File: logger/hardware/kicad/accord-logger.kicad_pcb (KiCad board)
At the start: 2 copper layers, 120 x 80 mm, 40 parts, among them J1 Board connector 14-way, J5 SD breakout 6-way, Q5 IPD50P04P4L-11, Q6 2N3904, Q7 2N3904, U1 RaspberryPi_Pico_W, U15 MAX3485, U16 DS3231SN, U6 LM2678T-5.0

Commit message: layout: rs485_links step placed and routed
Owner switched on rs485_links (R47-R49, JP2-JP4; six on_board flags).
JP2-JP4 sit in a row at the top edge (y 64), R47/R48 bias and R49
termination between them and U15. Nets checked pad by pad: R47 BIAS_HI-A,
R48 B-BIAS_LO, R49 A-TERM, JP2 TERM-B, JP3 3V3-BIAS_HI, JP4 BIAS_LO-PGND.

Scratch copy refilled: the front pour now has one 45.6 mm2 piece around
U15 (x 148-163, y 64-73) cut off by the new tracks; it is tied to ground
through U15 pin 5 and JP4's through-hole pads, and KiCad's island removal
(always) keeps only connected copper. Two slivers under 1 mm2. DRC
schematic parity 0, no clearance or courtyard errors; unconnected only
AGND (with the inputs) and Q5's middle lead (internal to the part).

Claude-Session-ID: 42dd0e33-28b5-4936-847e-9c2e1d2488fa
Co-Authored-By: Claude Opus 5.5 <noreply@anthropic.com>
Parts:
- added JP2: TERM default OPEN, Connector_PinHeader_2.54mm:PinHeader_1x02_P2.54mm_Vertical, F.Cu at (165.7, 64.1)
- added JP3: BIAS HI default OPEN, Connector_PinHeader_2.54mm:PinHeader_1x02_P2.54mm_Vertical, F.Cu at (169.5, 64.1)
- added JP4: BIAS LO default OPEN, Connector_PinHeader_2.54mm:PinHeader_1x02_P2.54mm_Vertical, F.Cu at (173.4, 64.1)
- added R47: 390R, Resistor_THT:R_Axial_DIN0207_L6.3mm_D2.5mm_P5.08mm_Vertical, F.Cu at (165.3, 71.8)
- added R48: 390R, Resistor_THT:R_Axial_DIN0207_L6.3mm_D2.5mm_P5.08mm_Vertical, F.Cu at (165.3, 75.6)
- added R49: 120R, Resistor_THT:R_Axial_DIN0207_L6.3mm_D2.5mm_P5.08mm_Vertical, F.Cu at (156.4, 66.0)
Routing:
- net /P3V3_SW: track 104.3 -> 138.0 mm
- net /RS485_B: track 55.2 -> 85.7 mm
- net /RS485_A: track 55.2 -> 83.1 mm
- net /RS485_BIAS_LO: track 0.00 -> 13.9 mm
- net /RS485_BIAS_HI: track 0.00 -> 6.83 mm
- net /RS485_TERM: track 0.00 -> 5.01 mm

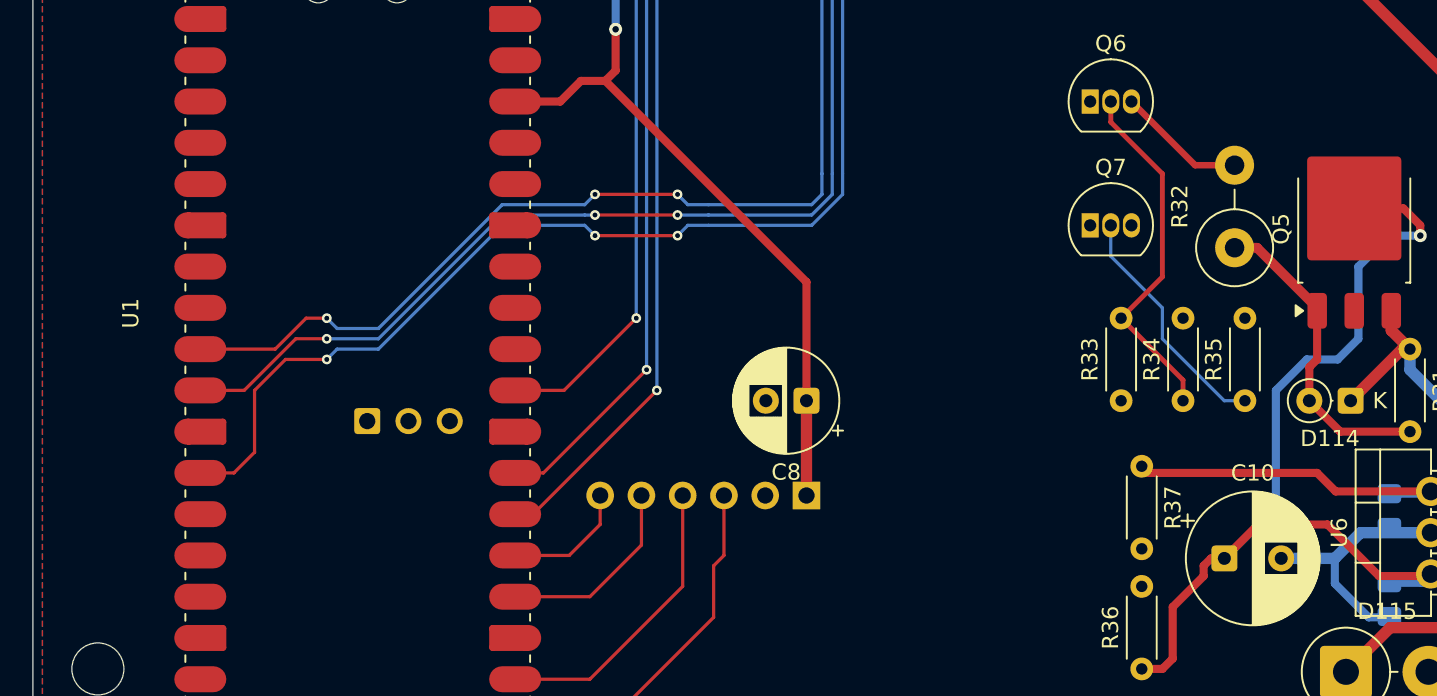
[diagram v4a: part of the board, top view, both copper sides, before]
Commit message: layout: headers step placed and routed
Owner switched on the headers step (J3, J4, TP24, TP25; four on_board
flags). J3 and the GP11/GP12 pads sit in the free strip left of the Pico
above the antenna end (J3 pin 4 at y 127.6, 7.3 mm from GP13); J4 is
13 mm from RUN. A missing via left U15 VCC, C24 and J3 pin 3 off 3V3 on
the first pass; with it added, a copper flood from U15 pin 8 reaches
every P3V3_SW pad including Pico pin 36.

Scratch copy refilled: DRC schematic parity 0, no clearance, courtyard
or dangling-track items; unconnected only AGND (with the inputs) and Q5's
middle lead (internal to the part). Saved with the zone unfilled.

Claude-Session-ID: 42dd0e33-28b5-4936-847e-9c2e1d2488fa
Co-Authored-By: Claude Opus 5.5 <noreply@anthropic.com>
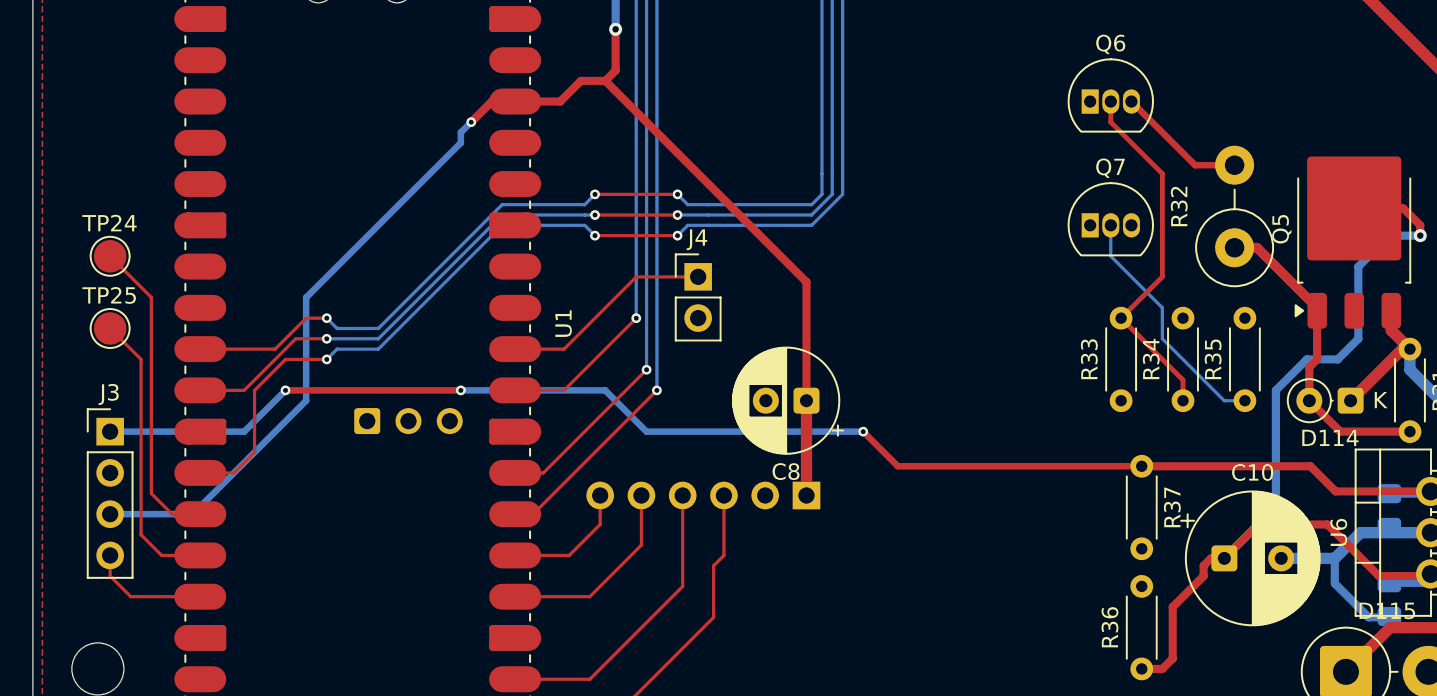
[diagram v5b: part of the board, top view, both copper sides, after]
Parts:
- added J3: Spare GP13 / switched power, Connector_PinHeader_2.54mm:PinHeader_1x04_P2.54mm_Vertical, F.Cu at (93.3, 120.0)
- added J4: Reset RUN-GND, Connector_PinHeader_2.54mm:PinHeader_1x02_P2.54mm_Vertical, F.Cu at (129.5, 110.5)
- added TP24: TestPoint, TestPoint:TestPoint_Pad_D2.0mm, F.Cu at (93.3, 109.2)
- added TP25: TestPoint, TestPoint:TestPoint_Pad_D2.0mm, F.Cu at (93.3, 113.7)
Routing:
- net /B5: track 53.0 -> 119.5 mm, vias 0 -> 3
- net /P3V3_SW: track 138.0 -> 177.6 mm, vias 3 -> 4
- net /SPARE_GP11: track 0.00 -> 19.2 mm
- net /SPARE_GP12: track 0.00 -> 17.7 mm
- net /RUN: track 0.00 -> 13.1 mm
- net /SPARE_GP13: track 0.00 -> 7.35 mm

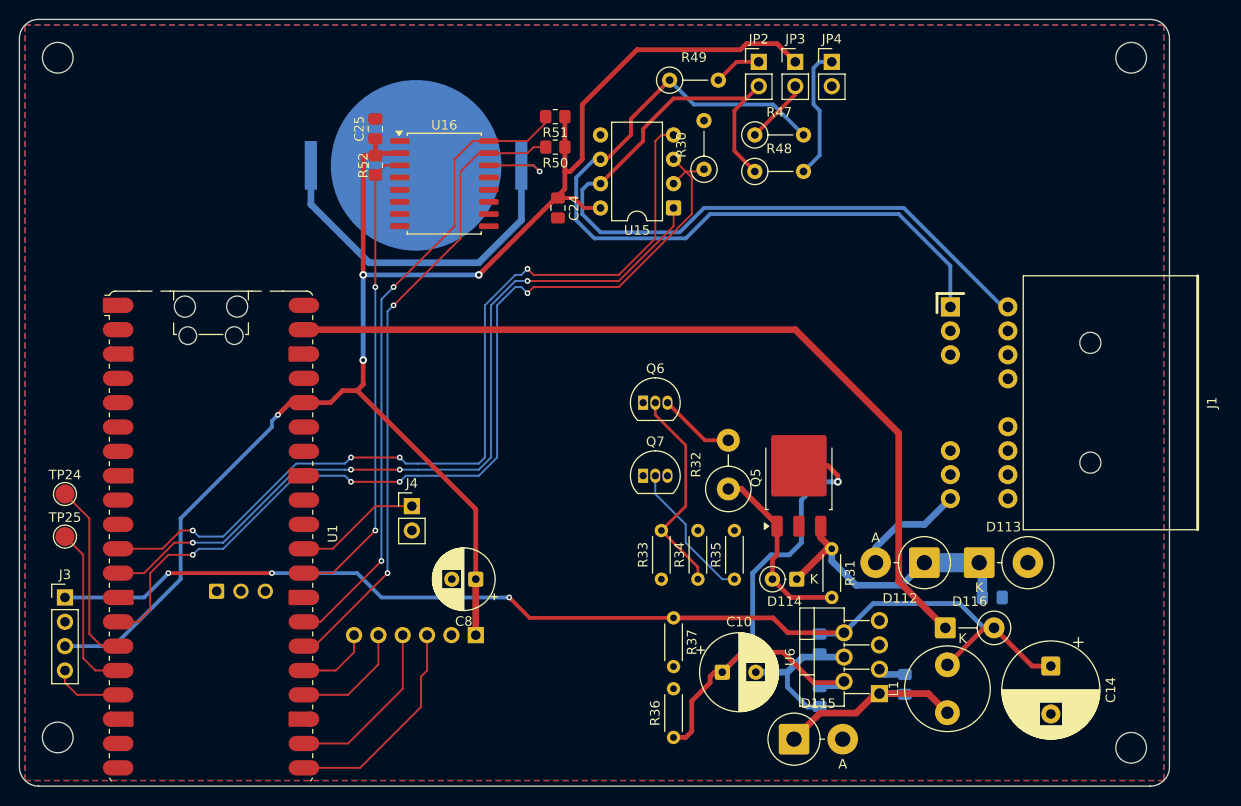
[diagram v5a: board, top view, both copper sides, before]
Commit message: layout: power_tps step placed and routed
Owner switched on power_tps (TP1-TP7, TP21-TP23; ten on_board flags) and
placed each beside its source; D115 moved 1.9 mm left (K to U6.1
11.8 mm, A to C10- 10.0 mm). Copper flood from each test point reaches
its net's parts: TP1 P12 (Q5.3, D112-D114, C9), TP2 GATE, TP3 VIN_SW
(U6.2, C10, C11), TP4 SW (4.5 mm stub), TP5 B5, TP6 VSYS, TP7 3V3 (all
12 pads), TP23 AGND at Pico pin 33.

Open: clearance error, the 0.2 mm B.Cu PGND track from (177.2, 123.8) to
TP22 passes about 0.13 mm from U6 pin 5 (NC); TP22 is a through-hole loop
on the pour, so the track can go. Otherwise DRC (refilled scratch copy)
parity 0; unconnected only AGND to J1.10 (with the inputs) and Q5's
middle lead.

Claude-Session-ID: 42dd0e33-28b5-4936-847e-9c2e1d2488fa
Co-Authored-By: Claude Opus 5.5 <noreply@anthropic.com>
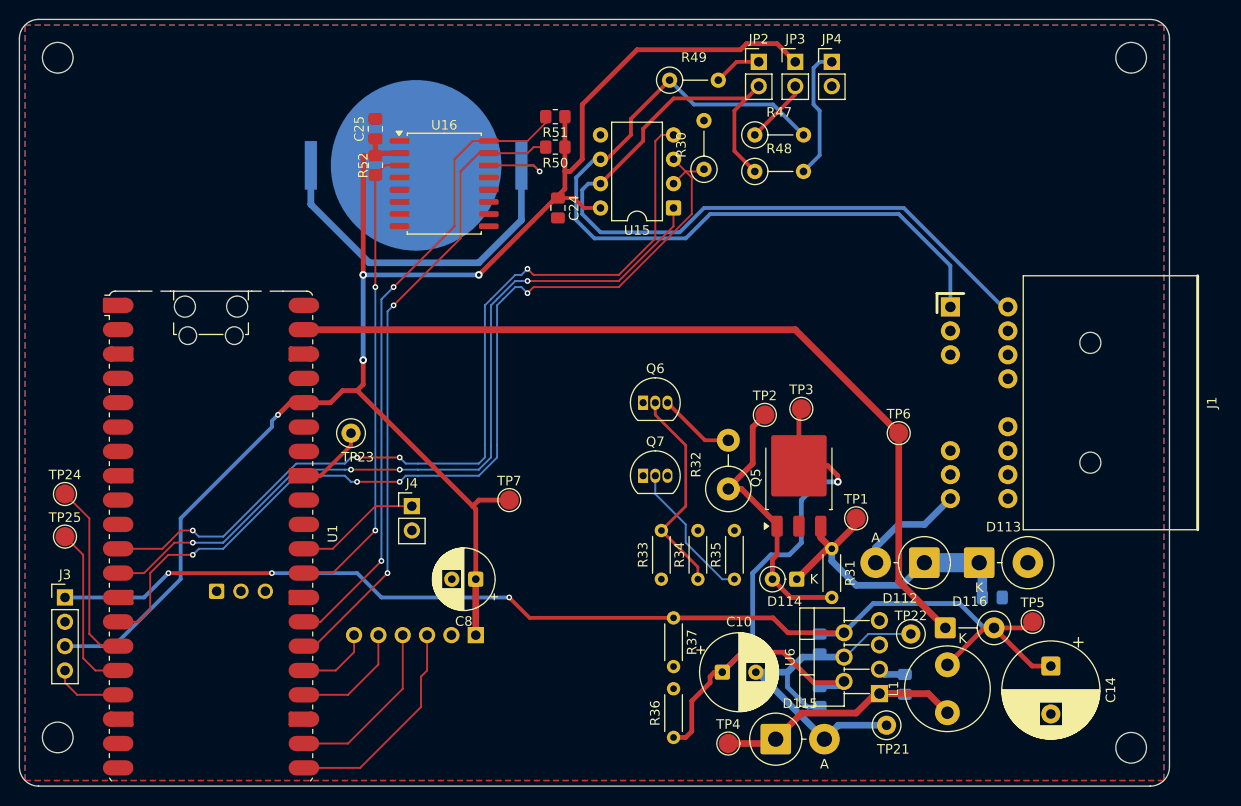
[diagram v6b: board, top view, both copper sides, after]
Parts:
- added TP1: TestPoint, TestPoint:TestPoint_Pad_D2.0mm, F.Cu at (175.9, 111.8)
- added TP2: TestPoint, TestPoint:TestPoint_Pad_D2.0mm, F.Cu at (166.4, 101.0)
- added TP21: TestPoint, TestPoint:TestPoint_Loop_D2.50mm_Drill1.0mm, F.Cu at (179.1, 133.3)
- added TP22: TestPoint, TestPoint:TestPoint_Loop_D2.50mm_Drill1.0mm, F.Cu at (181.6, 123.8)
- added TP23: TestPoint, TestPoint:TestPoint_Loop_D2.50mm_Drill1.0mm, F.Cu at (123.2, 102.9)
- added TP3: TestPoint, TestPoint:TestPoint_Pad_D2.0mm, F.Cu at (170.2, 100.3)
- added TP4: TestPoint, TestPoint:TestPoint_Pad_D2.0mm, F.Cu at (162.6, 135.3)
- added TP5: TestPoint, TestPoint:TestPoint_Pad_D2.0mm, F.Cu at (194.3, 122.6)
- added TP6: TestPoint, TestPoint:TestPoint_Pad_D2.0mm, F.Cu at (180.3, 102.9)
- added TP7: TestPoint, TestPoint:TestPoint_Pad_D2.0mm, F.Cu at (139.7, 109.9)
- moved D115 1.91 mm to (167.5, 134.8)
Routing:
- net /PGND: track 15.6 -> 40.8 mm
- net /GATE: track 19.5 -> 28.8 mm
- net /AGND: track 0.00 -> 7.50 mm
- net /SW: track 21.5 -> 28.5 mm
- net /VIN_SW: track 60.1 -> 66.1 mm
- net /B5: track 119.5 -> 123.8 mm
- net /P12: track 30.3 -> 34.5 mm
- net /P3V3_SW: track 177.6 -> 181.7 mm

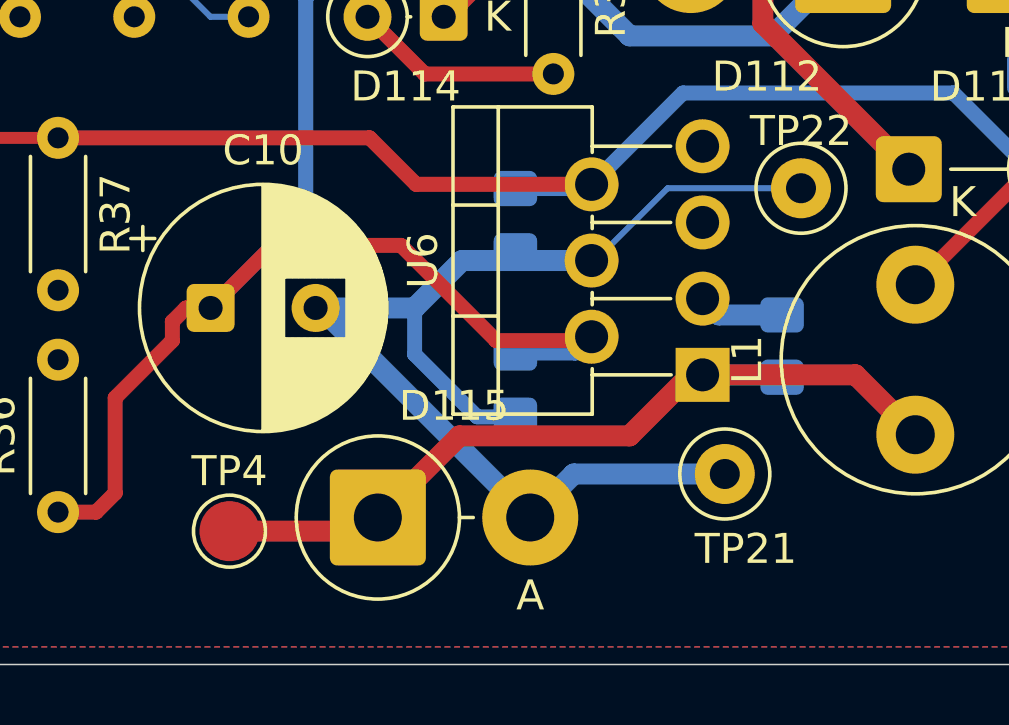
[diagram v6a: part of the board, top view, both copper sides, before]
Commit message: layout: TP4 moved beside U6, TP22 clearance fixed
TP4 (SW) now sits by U6 with about 1.8 mm of stub (was 4.5 mm); the
PGND track that crowded U6 pin 5 is gone and TP21 shifted 0.6 mm. Saved
with the pour filled. DRC: no clearance errors, parity 0, unconnected
only AGND to J1.10 and Q5's middle lead.

Claude-Session-ID: 42dd0e33-28b5-4936-847e-9c2e1d2488fa
Co-Authored-By: Claude Opus 5.5 <noreply@anthropic.com>
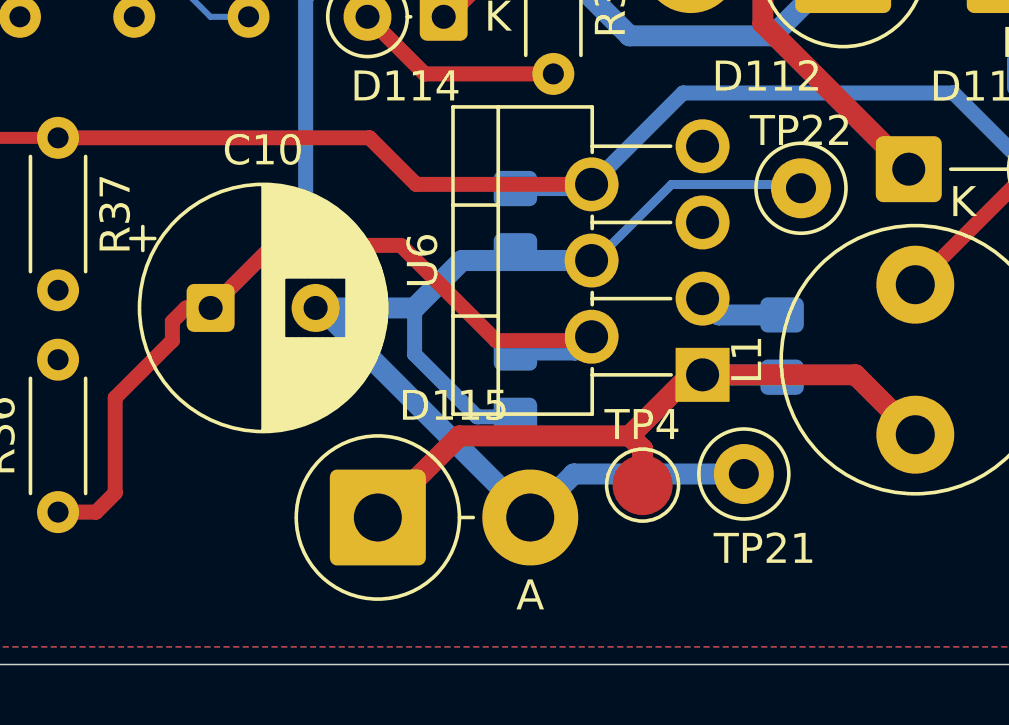
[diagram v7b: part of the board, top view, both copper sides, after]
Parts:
- moved TP4 13.9 mm to (176.3, 133.7)
- moved TP21 0.64 mm to (179.7, 133.3)
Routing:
- net /SW: track 28.5 -> 25.9 mm
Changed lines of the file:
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@@
 	(footprint "TestPoint:TestPoint_Pad_D2.0mm"
 		(layer "F.Cu")
-		(at 162.56 135.255)
+		(at 176.33 133.72)
 		(descr "SMD pad as test Point, diameter 2.0mm")
 		(tags "test point SMD pad")
@@
 	(footprint "TestPoint:TestPoint_Loop_D2.50mm_Drill1.0mm"
 		(layer "F.Cu")
-		(at 179.07 133.35)
+		(at 179.705 133.35)
 		(descr "wire loop as test point, loop diameter 2.5mm, hole diameter 1.0mm")
 		(tags "test point wire loop bead")
@@
 	)
 	(segment
+		(start 177.8 123.7)
+		(end 181.61 123.7)
+		(width 0.3)
+		(layer "B.Cu")
+		(net 4)
+	)
+	(segment
 		(start 174.63 126.234823)
 		(end 174.755177 126.234823)
@@
 	)
 	(segment
+		(start 174.755177 126.234823)
+		(end 177.29 123.7)
+		(width 0.3)
+		(layer "B.Cu")
+		(net 4)
+	)
+	(segment
 		(start 168.73 127.815)
 		(end 165.43 127.815)
@@
 	)
 	(segment
-		(start 177.165 123.825)
-		(end 181.61 123.825)
-		(width 0.2)
-		(layer "B.Cu")
-		(net 4)
-	)
-	(segment
 		(start 172.585 134.8)
 		(end 174.035 133.35)
@@
 	)
 	(segment
-		(start 174.755177 126.234823)
-		(end 177.165 123.825)
-		(width 0.2)
-		(layer "B.Cu")
-		(net 4)
-	)
-	(segment
 		(start 170.310177 126.234823)
 		(end 168.73 127.815)
@@
 	)
 	(segment
+		(start 177.29 123.7)
+		(end 177.8 123.7)
+		(width 0.3)
+		(layer "B.Cu")
+		(net 4)
+	)
+	(segment
 		(start 121.0525 99.695)
 		(end 118.275 99.695)
@@
 	)
 	(segment
-		(start 167.05 135.255)
-		(end 162.56 135.255)
+		(start 175.895 132.08)
+		(end 176.33 132.515)
 		(width 0.7)
 		(layer "F.Cu")
@@
 	)
 	(segment
+		(start 176.33 132.515)
+		(end 176.33 133.72)
+		(width 0.7)
+		(layer "F.Cu")
+		(net 9)
+	)
+	(segment
 		(start 175.895 132.08)
 		(end 177.930177 130.044823)
@@
 		(min_thickness 0.25)
 		(filled_areas_thickness no)
-		(fill
+		(fill yes
 			(thermal_gap 0.5)
 			(thermal_bridge_width 0.5)
